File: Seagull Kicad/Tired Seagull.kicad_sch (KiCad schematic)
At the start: 37 parts, among them SW1 PCM12SMTR, U1 nice_nano

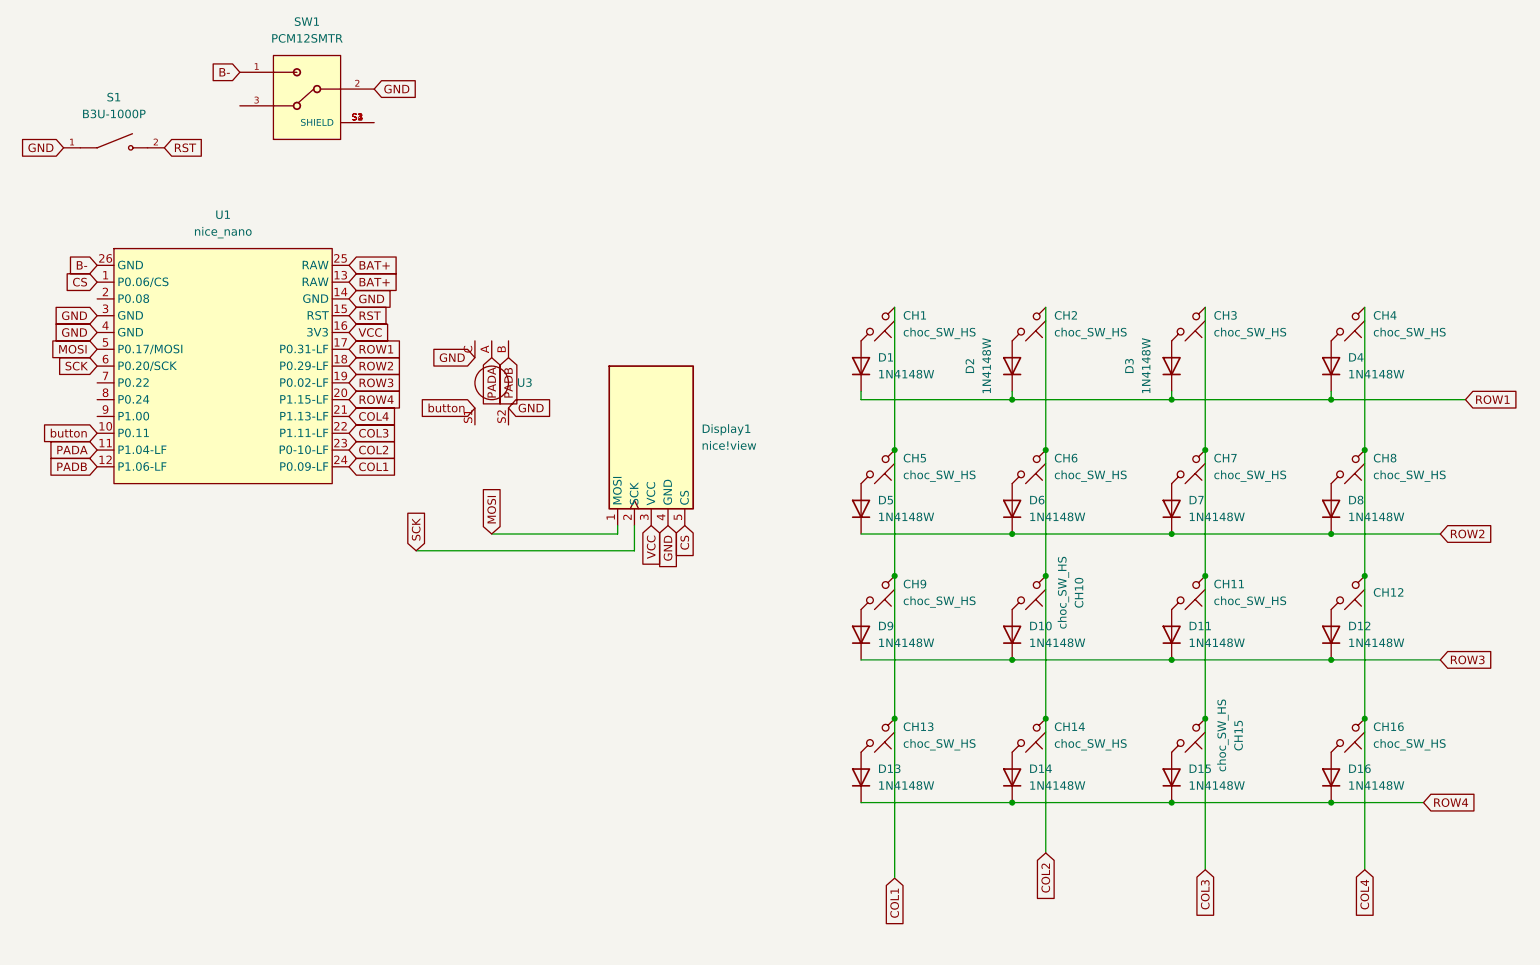
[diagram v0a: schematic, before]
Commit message: V3 Commit
Added diode for encoder as VIAL does not support direct key, must be in a matrix.
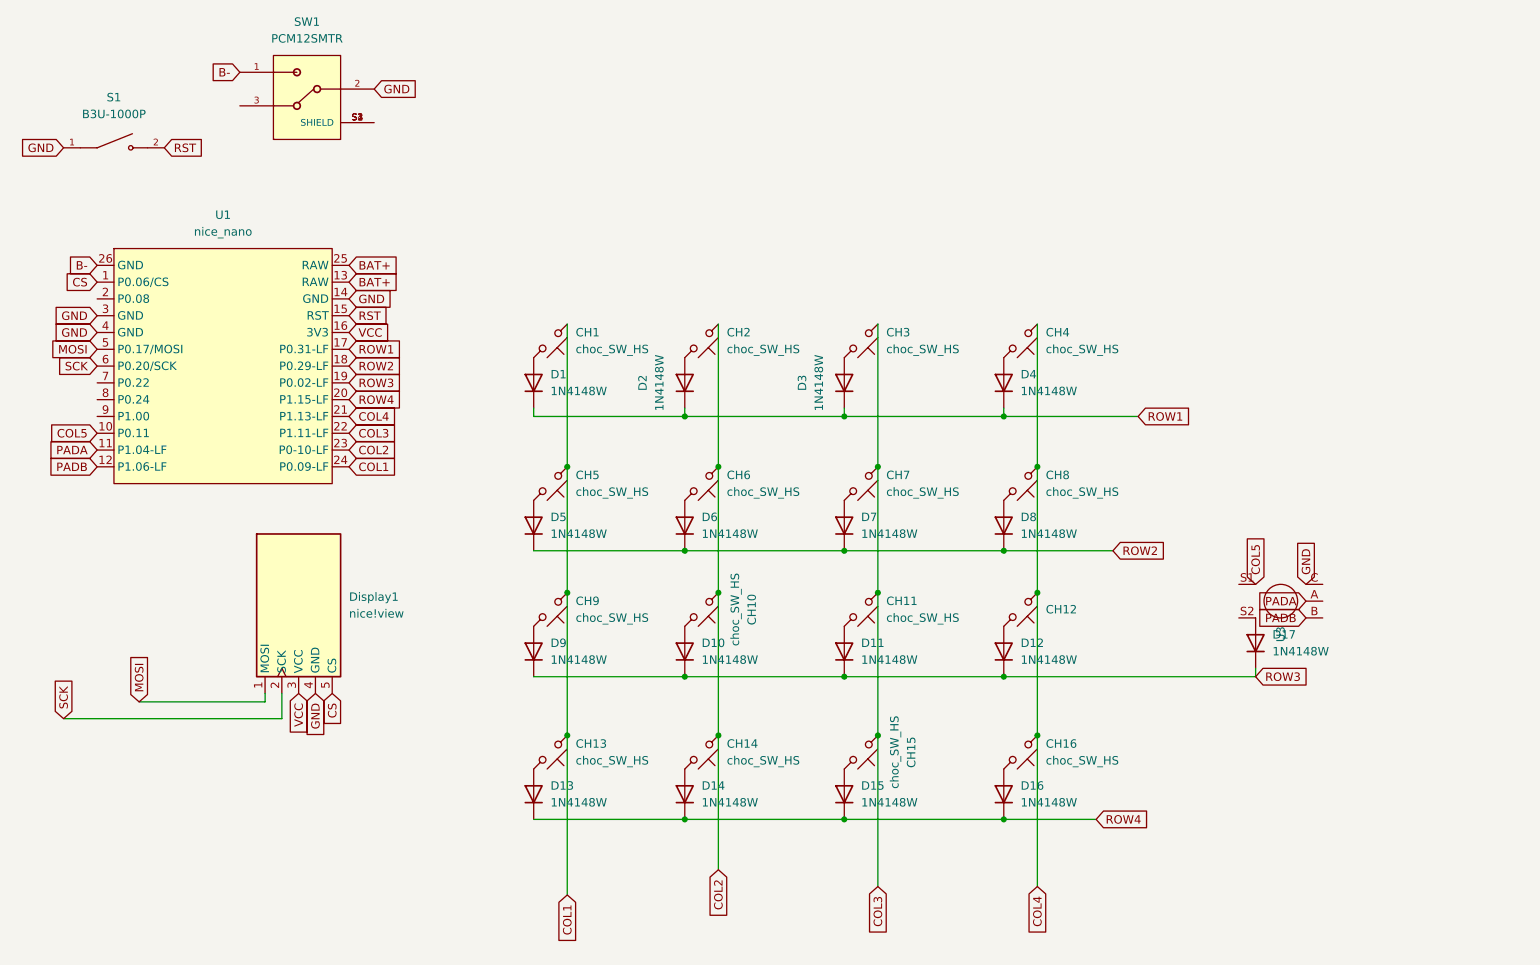
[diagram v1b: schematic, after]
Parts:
- added D17: 1N4148W, Diode_SMD:D_SOD-123, symbol Diode:1N4148W
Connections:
- net GND: no longer U3.S2
- net ROW3: now also D17.1 (K)
- net button renamed COL5
- new net: D17.2 (A), U3.S2
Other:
- moved on the sheet: CH1, CH10, CH11, CH12, CH13, CH14, CH15, CH16, CH2, CH3, CH4, CH5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
